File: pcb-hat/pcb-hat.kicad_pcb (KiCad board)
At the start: 4 copper layers, 54.5 x 55 mm, 65 parts, among them Q1 NTMFS5C468NLT1G, Q2 Q_NPN, Q3 Q_PMOS_GSD, U1 AOZ6605PI-1, U2 INA219AxD, U3 INA219AxD, U4 HTD Servo, U5 Vertical_Pi_Breakout, U6 Power_Connector, U7 AOZ6605PI-1, U8 Horizontal_Pi_Breakout, U9 Raspberry_Pi_Generic

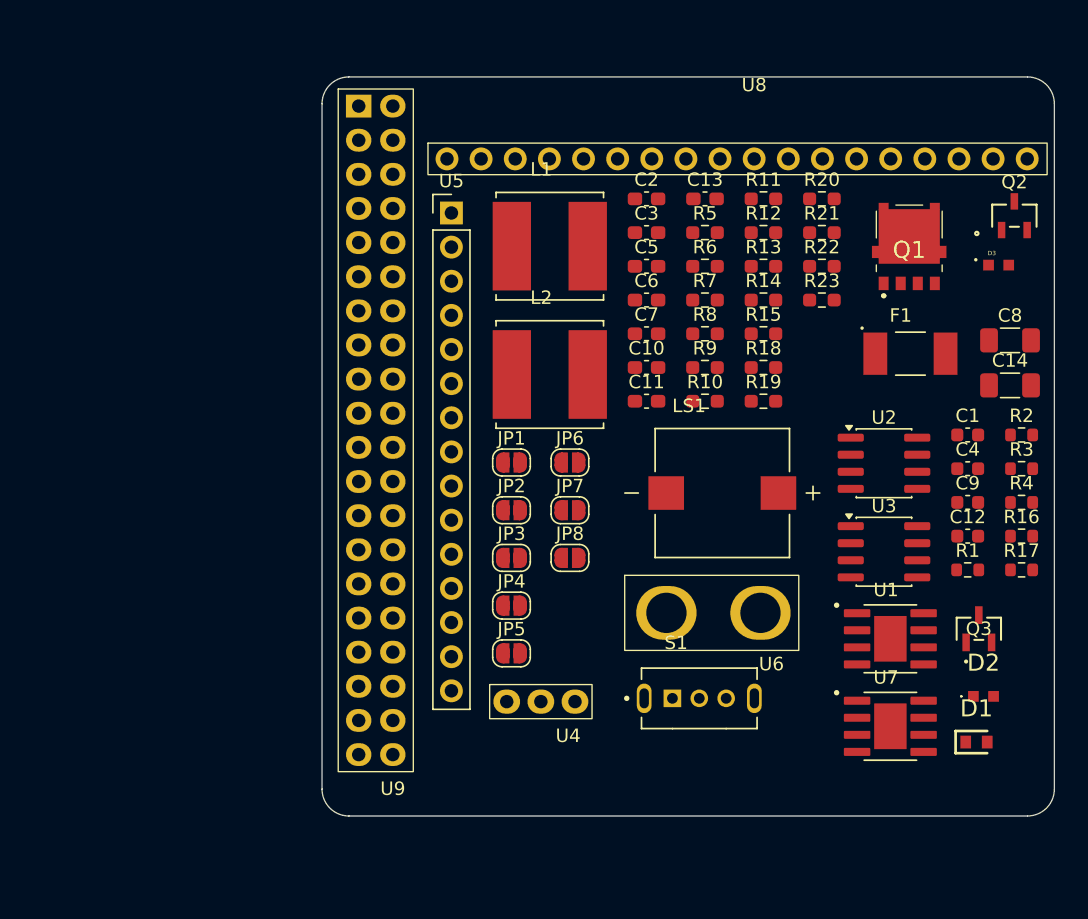
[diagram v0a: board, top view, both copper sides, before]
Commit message: WIP: Fix footprints, add new jumper pad, 3d models. Begin routing
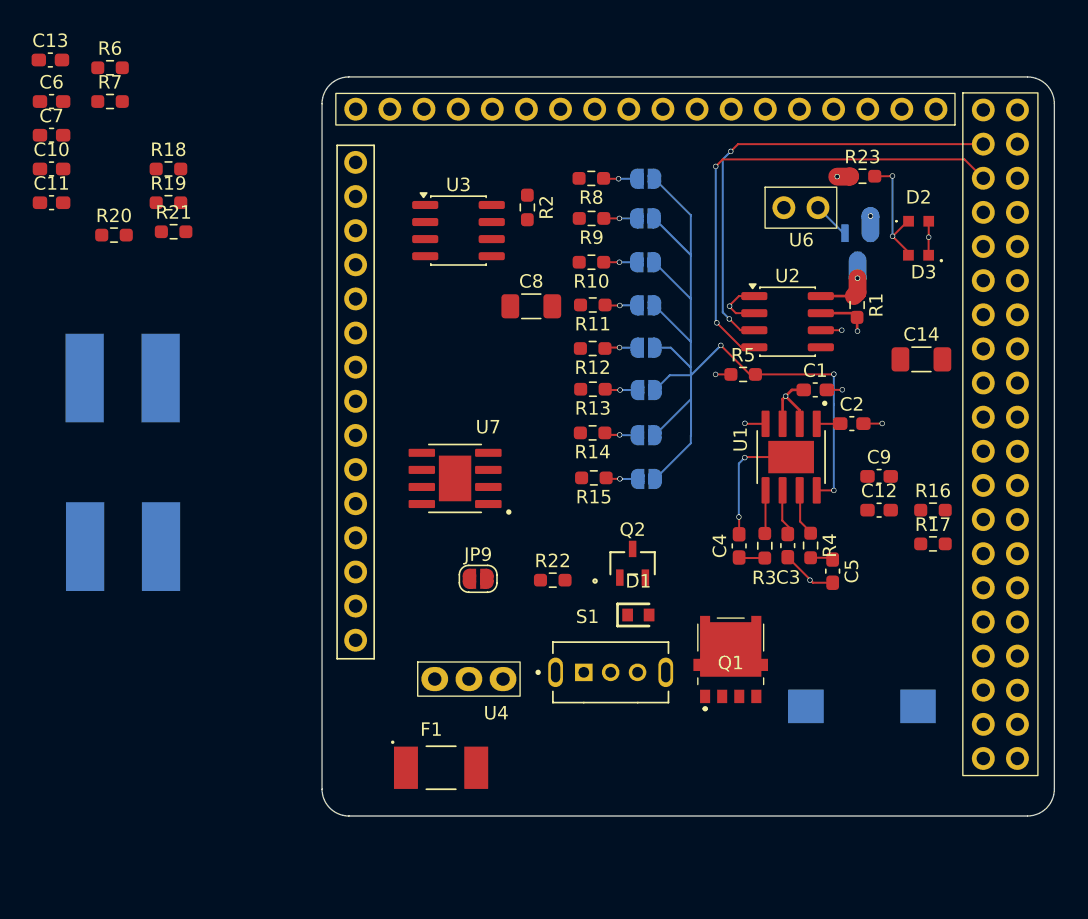
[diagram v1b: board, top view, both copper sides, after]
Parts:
- added JP9: TX to RX?, Jumper:SolderJumper-2_P1.3mm_Open_RoundedPad1.0x1.5mm, F.Cu at (109.1, 100.3)
- C1, C12, C4, C9: footprint Capacitor_SMD:C_0603_1608Metric -> Capacitor_SMD:C_0603_1608Metric_Pad1.08x0.95mm_HandSolder
- JP1, JP2, JP3, JP4, JP5, JP6, JP7, JP8, L1, L2, LS1, Q3: moved to B.Cu
- R1, R16, R17, R2, R3, R4: footprint Resistor_SMD:R_0603_1608Metric -> Resistor_SMD:R_0603_1608Metric_Pad0.98x0.95mm_HandSolder
- U5: footprint Connector_PinHeader_2.54mm:PinHeader_1x15_P2.54mm_Vertical -> pcb_hat:vertical_pi_breakout
- moved R20 52.8 mm to (82.0, 74.8)
- moved C13 49.8 mm to (77.3, 61.7)
- moved R21 48.2 mm to (86.5, 74.5)
- moved U9 47.1 mm to (147.9, 89.4)
- moved C10 46.7 mm to (77.4, 69.8)
- moved C11 46.7 mm to (77.4, 72.4)
- moved C6 46.7 mm to (77.4, 64.8)
- moved C7 46.7 mm to (77.4, 67.3)
- moved R6 46.7 mm to (81.7, 62.3)
- moved R7 46.7 mm to (81.7, 64.8)
- moved R18 46.7 mm to (86.1, 69.8)
- moved R19 46.7 mm to (86.1, 72.4)
- moved F1 46.6 mm to (106.4, 114.4)
- moved R2 40.5 mm to (112.8, 72.7), turned to -90 degrees
- moved U3 39.7 mm to (107.7, 74.4)
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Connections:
- Q2 pad 1: (no net) -> Net-(Q2-B)
- Q2 pad 2: (no net) -> GND
- Q2 pad 3: (no net) -> Net-(D1-A)
- R18 pad 2: Net-(Q2-PadB) -> Net-(Q2-B)
- R19 pad 1: Net-(Q2-PadB) -> Net-(Q2-B)
- R6 pad 2: /Pi_RX_Out -> Net-(JP9-B)
- S1 pad 1: /Pi_RX_Out -> Net-(JP9-B)
- U9 pad 14: (no net) -> GND
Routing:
- net /V_Choose: track 0.00 -> 69.2 mm, vias 0 -> 3
- net /Pi_SCL: track 0.00 -> 35.9 mm, vias 0 -> 2
- net /Pi_SDA: track 0.00 -> 34.4 mm, vias 0 -> 2
- net GND: track 0.00 -> 20.6 mm, vias 0 -> 8
- net VCC_LOAD: track 0.00 -> 10.8 mm, vias 0 -> 2
- net Net-(D2-K): track 0.00 -> 9.37 mm, vias 0 -> 2
- net Net-(U1-LX): track 0.00 -> 9.36 mm, vias 0 -> 2
- net VCC: track 0.00 -> 5.22 mm, vias 0 -> 1
- net Net-(U1-COMP): track 0.00 -> 3.53 mm
- net Net-(U1-VCC): track 0.00 -> 3.51 mm
- net Net-(U1-BST): track 0.00 -> 3.24 mm
- net Net-(JP5-B): track 0.00 -> 2.51 mm, vias 0 -> 1
- net Net-(JP1-B): track 0.00 -> 2.50 mm, vias 0 -> 1
- net Net-(JP7-B): track 0.00 -> 2.49 mm, vias 0 -> 1
- net Net-(JP3-B): track 0.00 -> 2.46 mm, vias 0 -> 1
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- added copper zone on In1.Cu, net +BATT
- added copper zone on In2.Cu, net GND
- added copper zone on In1.Cu, net VCC_LOAD

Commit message: Finish PCB design v0.1
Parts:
- removed the R6 at (81.7, 62.3)
- removed S1: SLW-864587-2A-RA-N-D, pcb_hat:SW_SLW-864587-2A-RA-N-D
- removed the U5 at (100.0, 69.4)
- removed U8: Horizontal_Pi_Breakout, pcb_hat:horizontal_breakout_footprint
- added G***: LOGO, pcb_hat:club_logo, B.Cu at (123.2, 110.4)
- added JP2: Servo Selector, Jumper:SolderJumper-3_P1.3mm_Open_RoundedPad1.0x1.5mm, F.Cu at (135.1, 105.9)
- added R7: 4k7, Resistor_SMD:R_0603_1608Metric_Pad0.98x0.95mm_HandSolder, F.Cu at (141.9, 98.8)
- added RPi5: RPi5, pcb_hat:Raspberry Pi 5, F.Cu at (123.4, 99.6)
- added kibuzzard-694E41B7: G***, kibuzzard-694E41B7, F.Cu at (136.4, 94.0)
- added kibuzzard-694E58A9: G***, kibuzzard-694E58A9, F.Cu at (132.2, 64.7)
- added kibuzzard-694E58BC: G***, kibuzzard-694E58BC, F.Cu at (139.2, 64.7)
- C14, C8: moved to B.Cu
- JP10: renamed from JP8; moved to F.Cu
- JP3: renamed from JP1; moved to F.Cu
- JP4: renamed from JP2; moved to F.Cu
- JP5: renamed from JP3; moved to F.Cu
- JP6: renamed from JP4; moved to F.Cu
- JP7: renamed from JP5; moved to F.Cu
- JP8: renamed from JP6; moved to F.Cu
- JP9: renamed from JP7; moved to F.Cu
- moved R6 76.3 mm to (142.2, 111.3), turned to 90 degrees
- moved C7 71.4 mm to (123.8, 121.6), turned to 180 degrees
- moved C13 65.7 mm to (140.9, 78.1), turned to 180 degrees
- moved C11 64.2 mm to (140.9, 81.6), turned to 180 degrees
- moved L2 58.0 mm to (135.3, 73.5), turned to 90 degrees
- moved R20 57.9 mm to (139.9, 76.2), turned to 180 degrees
- moved C10 52.5 mm to (129.2, 77.7), turned to 180 degrees
- moved R21 50.7 mm to (137.2, 76.2), turned to 90 degrees
- moved C6 50.7 mm to (123.6, 85.8), turned to -90 degrees
- moved U3 48.0 mm to (128.1, 117.8), turned to 90 degrees
- moved R2 42.6 mm to (127.2, 112.8), turned to 0 degrees
- moved L1 40.6 mm to (120.6, 99.8), turned to -90 degrees
- moved D1 33.3 mm to (127.3, 70.3), turned to 180 degrees
- moved R22 31.2 mm to (132.7, 75.0)
- moved JP1 30.9 mm to (139.5, 105.9), turned to 180 degrees
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- renumbered JP9 to JP1, R7 to R6, U6 to U5, U7 to U6, U9 to U7
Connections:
- U7 pad 11: /GPIO17 -> unconnected-(U7-GPIO17/GPIO_GEN0-Pad11)
- U7 pad 13: /GPIO27 -> unconnected-(U7-GPIO27/GPIO_GEN2-Pad13)
- U7 pad 15: /GPIO22 -> unconnected-(U7-GPIO22/GPIO_GEN3-Pad15)
- U7 pad 16: /GPIO23 -> unconnected-(U7-GPIO23/GPIO_GEN4-Pad16)
- U7 pad 18: /GPIO24 -> unconnected-(U7-GPIO24/GPIO_GEN5-Pad18)
- U7 pad 19: /GPIO10 -> unconnected-(U7-GPIO10/SPI_MOSI-Pad19)
- U7 pad 21: /GPIO9 -> unconnected-(U7-GPIO9/SPI_MISO-Pad21)
- U7 pad 22: /GPIO25 -> unconnected-(U7-GPIO25/GPIO_GEN6-Pad22)
- U7 pad 23: /GPIO11 -> unconnected-(U7-GPIO11/SPI_SCLK-Pad23)
- U7 pad 24: /GPIO8 -> unconnected-(U7-GPIO8/~{SPI_CE0}-Pad24)
- U7 pad 26: /GPIO7 -> unconnected-(U7-GPIO7/~{SPI_CE1}-Pad26)
- U7 pad 27: /ID_SD -> unconnected-(U7-ID_SD-Pad27)
- U7 pad 28: /ID_SC -> unconnected-(U7-ID_SC-Pad28)
- U7 pad 31: /GPIO6 -> unconnected-(U7-GPIO6-Pad31)
- U7 pad 32: /GPIO12 -> unconnected-(U7-GPIO12-Pad32)
- U7 pad 33: /GPIO13 -> unconnected-(U7-GPIO13-Pad33)
- U7 pad 35: /GPIO19 -> unconnected-(U7-GPIO19-Pad35)
- U7 pad 36: /GPIO16 -> unconnected-(U7-GPIO16-Pad36)
- U7 pad 38: /GPIO20 -> unconnected-(U7-GPIO20-Pad38)
- U7 pad 40: /GPIO21 -> unconnected-(U7-GPIO21-Pad40)
- U7 pad 7: /GPIO4 -> unconnected-(U7-GPIO4/GPIO_GCKL-Pad7)
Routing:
- net +3V3: track 0.00 -> 146.9 mm, vias 0 -> 2
- net /Pi_SDA: track 34.4 -> 98.6 mm, vias 2 -> 4
- net /Pi_SCL: track 35.9 -> 95.5 mm, vias 2 -> 4
- net VDC_LOAD: track 0.00 -> 49.9 mm, vias 0 -> 4
- net /Pi_RX_Out: track 0.00 -> 45.1 mm, vias 0 -> 2
- net VDC: track 0.00 -> 43.4 mm, vias 0 -> 4
- net /GPIO18: track 0.00 -> 42.3 mm, vias 0 -> 2
- net GND: track 20.6 -> 56.7 mm, vias 8 -> 19
- net +5V: track 0.00 -> 35.9 mm, vias 0 -> 1
- net /V_Choose: track 69.2 -> 37.8 mm, vias 3 -> 0
- net /Pi_TX_Out: track 0.00 -> 30.6 mm, vias 0 -> 1
- net VCC_LOAD: track 10.8 -> 33.7 mm, vias 2 -> 3
- net Net-(D1-A): track 0.00 -> 17.5 mm
- net Net-(JP1-B): track 0.00 -> 10.5 mm
- net /BUZZER_PIN: track 0.00 -> 9.73 mm
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- added copper zone on In2.Cu, net +BATT
- added copper zone on In1.Cu, net GND
- added copper zone on B.Cu, net Net-(U1-LX)
- added copper zone on F.Cu, net Net-(U1-LX)
- added copper zone on B.Cu, net Net-(U6-LX)
- added copper zone on F.Cu, net Net-(U6-LX)
- added copper zone on In2.Cu, net VDC
- removed copper zone on In1.Cu, net +BATT
- removed copper zone on In2.Cu, net GND
- removed copper zone on In1.Cu, net VCC_LOAD
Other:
- board size 54.5 x 55 mm -> 40.9 x 60.1 mm
- board text added: "+"
- board text added: "-"
- board text added: "18V-5A"
- board text added: "Max"
- board text added: "New"
- board text added: "Old"
- board text added: "S"
- board text added: "Servo Voltage Selector"
- board text added: "v0.1"

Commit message: Fix blue LED not turning on
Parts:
- R18: value 10k -> 8.2k
- R19: value 100k -> 1k
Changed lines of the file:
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@@
 			)
 		)
-		(property "Value" "100k"
+		(property "Value" "1k"
 			(at 0 1.43 90)
 			(layer "F.Fab")
@@
 			)
 		)
-		(property "Value" "10k"
+		(property "Value" "8.2k"
 			(at 0 1.43 90)
 			(layer "F.Fab")

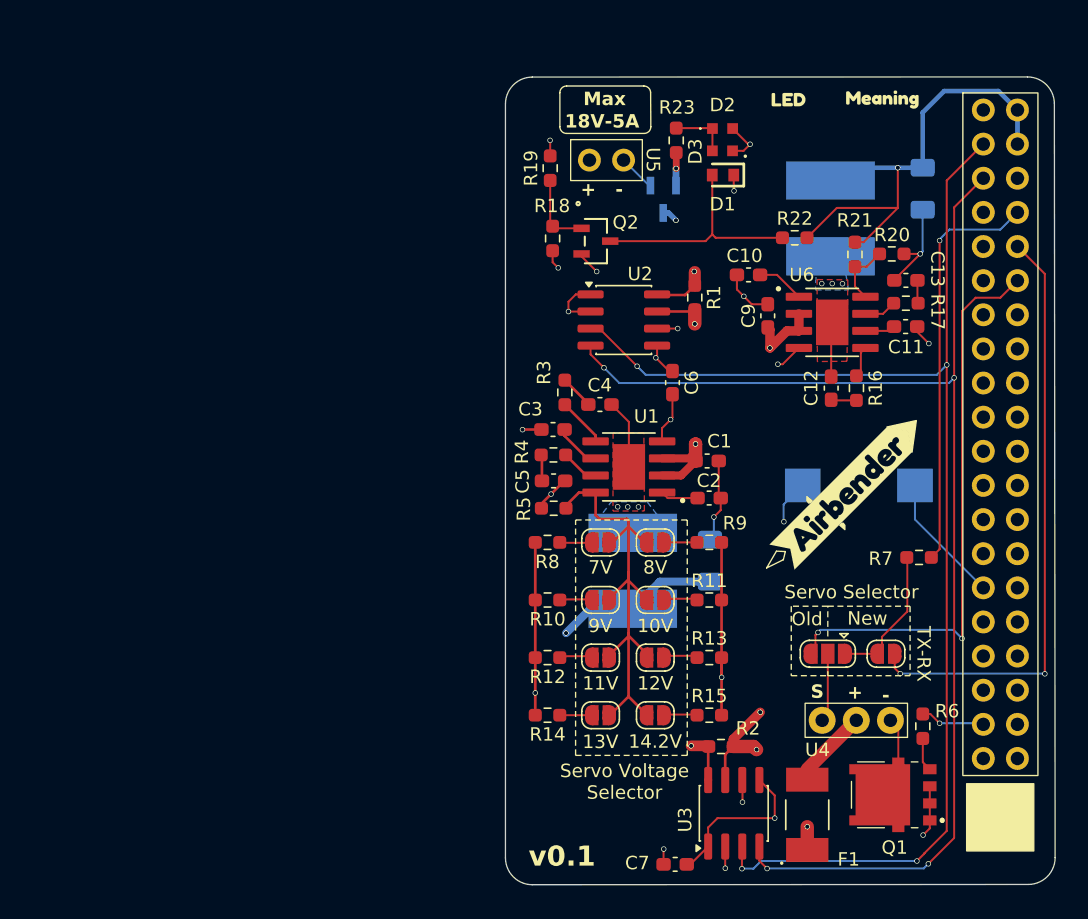
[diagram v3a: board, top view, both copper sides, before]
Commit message: Update schematic and reroute PCB
See the github PR for all changes
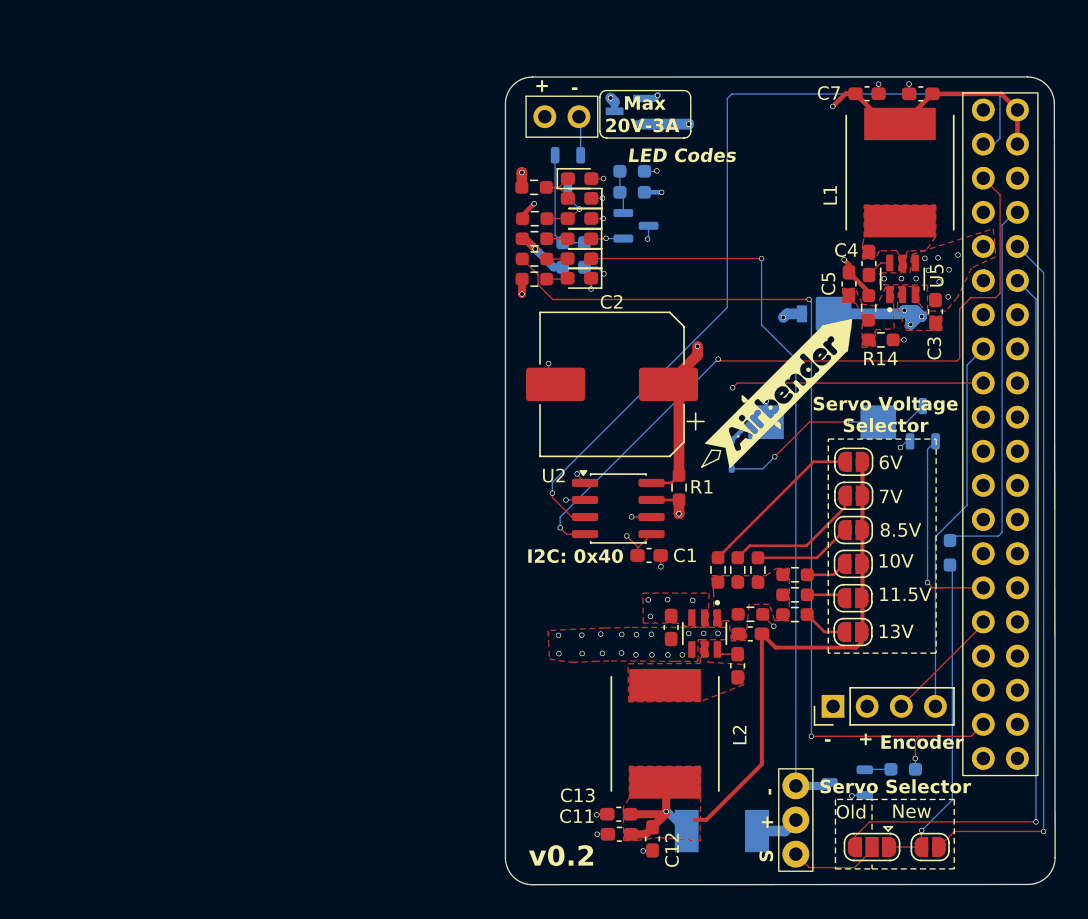
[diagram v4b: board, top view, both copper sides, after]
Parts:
- removed the C1 at (126.2, 91.6)
- removed C14: 47u, Capacitor_SMD:C_1206_3216Metric_Pad1.33x1.80mm_HandSolder
- removed JP10, JP9: SolderJumper_2_Open, Jumper:SolderJumper-2_P1.3mm_Open_RoundedPad1.0x1.5mm
- removed the Q3 at (122.9, 72.1)
- removed the R16 at (137.3, 86.2)
- removed the R17 at (140.9, 79.8)
- removed the R2 at (127.2, 112.8)
- removed the R20 at (139.9, 76.2)
- removed the R21 at (137.2, 76.2)
- removed the R3 at (115.6, 86.5)
- removed the R4 at (114.7, 91.1)
- removed the R5 at (114.7, 95.1)
- removed the U1 at (120.3, 92.0)
- removed the U3 at (128.1, 117.8)
- removed kibuzzard-694E58A9: G***, kibuzzard-694E58A9
- removed kibuzzard-694E58BC: G***, kibuzzard-694E58BC
- added C6: 22u, Capacitor_SMD:C_0603_1608Metric_Pad1.08x0.95mm_HandSolder, F.Cu at (142.1, 64.3)
- added D4: SS3P4-M3/84A, Diode_SMD:D_SMP_DO-220AA, B.Cu at (134.9, 80.6)
- added D5: LED_Small, LED_SMD:LED_0603_1608Metric_Pad1.05x0.95mm_HandSolder, F.Cu at (116.6, 75.0)
- added D6: 1N4148WS, Diode_SMD:D_SOD-323, B.Cu at (128.0, 91.1)
- added D7: LED_Small, LED_SMD:LED_0603_1608Metric_Pad1.05x0.95mm_HandSolder, F.Cu at (116.6, 76.5)
- added D8: LED_Small, LED_SMD:LED_0603_1608Metric_Pad1.05x0.95mm_HandSolder, F.Cu at (116.7, 78.0)
- added Q1: Q_PMOS_GSD, pcb_hat:SOT_7DS-T1-GE3_VIS, B.Cu at (120.3, 65.6)
- added Q4: 2N7002K_R1_00001, Package_TO_SOT_SMD:TSOT-23, B.Cu at (142.2, 88.8)
- added R10: 10k, Resistor_SMD:R_0603_1608Metric_Pad0.98x0.95mm_HandSolder, B.Cu at (120.6, 70.0)
- added R11: 1k, Resistor_SMD:R_0603_1608Metric_Pad0.98x0.95mm_HandSolder, F.Cu at (113.3, 76.5)
- added R12: 2k, Resistor_SMD:R_0603_1608Metric_Pad0.98x0.95mm_HandSolder, F.Cu at (113.3, 78.0)
- added R13: 162k, Resistor_SMD:R_0603_1608Metric_Pad0.98x0.95mm_HandSolder, F.Cu at (138.2, 80.2)
- added R8: 2k, Resistor_SMD:R_0603_1608Metric_Pad0.98x0.95mm_HandSolder, F.Cu at (113.3, 75.0)
- added R9: 9.1k, Resistor_SMD:R_0603_1608Metric_Pad0.98x0.95mm_HandSolder, B.Cu at (120.6, 71.6)
- added U4: TL431DBZ, Package_TO_SOT_SMD:SOT-23, B.Cu at (120.9, 74.1)
- added U5: AP63300WU-7, pcb_hat:SOT95P280X100-6N, F.Cu at (140.7, 78.0)
- added U7: AP63300WU-7, pcb_hat:SOT95P280X100-6N, F.Cu at (126.0, 104.4)
- C10: value 22n -> 12p
- C11: value 1u -> 22u
- C12: value 0.1u -> 22u
- C13: value 0.012u -> 22u
- C2: value 22n -> 1000u; footprint Capacitor_SMD:C_0603_1608Metric_Pad1.08x0.95mm_HandSolder -> Capacitor_SMD:CP_Elec_10x10.5
- C3: value 1u -> 10u
- C4: value 0.1u -> 100n
- C5: value 0.012u -> 47p
- C7: value 100n -> 22u
- C8: value 47u -> 10u; footprint Capacitor_SMD:C_1206_3216Metric_Pad1.33x1.80mm_HandSolder -> Capacitor_SMD:C_0603_1608Metric_Pad1.08x0.95mm_HandSolder; moved to F.Cu
- C9: value 22u -> 100n
- D1: renamed from D2; footprint pcb_hat:LEDLSQ97601N1Q21 -> LED_SMD:LED_0603_1608Metric_Pad1.05x0.95mm_HandSolder
- D2: renamed from D3; footprint pcb_hat:LEDM1608X80 -> LED_SMD:LED_0603_1608Metric_Pad1.05x0.95mm_HandSolder
- D3: renamed from D1; footprint pcb_hat:LEDC1608X35N -> LED_SMD:LED_0603_1608Metric_Pad1.05x0.95mm_HandSolder
- F1: moved to B.Cu
- L1, L2: value SRN8040TA-4R7M -> 6.8u; footprint pcb_hat:IND_SRN8040TA-4R7M -> pcb_hat:IND_ETQP4M6R8KVK; moved to F.Cu
- LS1: value SMI-1027-T-5V-R -> ~
- Q2: footprint pcb_hat:MTR_MMBT2222A-TP_MCE -> Package_TO_SOT_SMD:TSOT-23; moved to B.Cu
- Q3: renamed from Q1; value NTMFS5C468NLT1G -> PJA3404A_R1_00001; footprint pcb_hat:NRVTS10100EMFST1G -> Package_TO_SOT_SMD:TSOT-23; moved to B.Cu
- R14: value 310k -> 30.1k
- R15: value 340k -> 30.1k
- R16: renamed from R8; value 160k -> 196k
- R17: renamed from R9; value 184k -> 233k
- R18: renamed from R10; value 210k -> 290k
- R19: renamed from R11; value 235k -> 346k
- R20: renamed from R12; value 260k -> 403k
- R21: renamed from R13; value 285k -> 459k
- R3: renamed from R18; moved to B.Cu
- R4: renamed from R19; moved to B.Cu
- R6: renamed from R7; moved to B.Cu
- R7: renamed from R6; moved to B.Cu
- U1: renamed from U5; value Power_Connector -> Headers
- U6: value AOZ6605PI-1 -> ~; footprint pcb_hat:SOIC127P600X170-9N -> Connector_PinHeader_2.54mm:PinHeader_1x04_P2.54mm_Vertical
- moved C7 59.1 mm to (138.1, 64.2), turned to 0 degrees
- moved C13 45.1 mm to (119.6, 117.9)
- moved C11 43.4 mm to (119.6, 119.4)
- moved L2 40.3 mm to (123.0, 111.9), turned to -90 degrees
- moved R14 37.4 mm to (139.1, 82.6), turned to 0 degrees
- moved C12 36.1 mm to (122.1, 119.7), turned to -90 degrees
- moved L1 35.7 mm to (140.5, 70.1), turned to 90 degrees
- moved C3 29.8 mm to (143.2, 80.5), turned to 90 degrees
- moved U6 28.6 mm to (135.5, 109.8), turned to 90 degrees
- moved C10 26.7 mm to (129.4, 104.5)
- moved C5 26.4 mm to (136.7, 78.4), turned to -90 degrees
- moved C9 26.1 mm to (128.4, 106.8), turned to -90 degrees
- moved C4 22.6 mm to (138.2, 76.9), turned to 90 degrees
- moved JP3 19.8 mm to (137.1, 91.6), turned to 0 degrees
- moved JP5 19.5 mm to (137.1, 96.7), turned to 0 degrees
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- renumbered C6 to C1, R23 to R2, R22 to R5, U4 to U3, U7 to U8
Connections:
- C10 pad 1: Net-(U6-SS) -> VDC
- C10 pad 2: GND -> /V_Choose
- C11 pad 1: GND -> VDC
- C11 pad 2: Net-(U6-VCC) -> GND
- C12 pad 1: Net-(C12-Pad1) -> VDC
- C12 pad 2: Net-(U6-LX) -> GND
- C13 pad 1: Net-(C13-Pad1) -> VDC
- C2 pad 1: Net-(U1-SS) -> VCC
- C3 pad 1: GND -> Net-(D4-K)
- C3 pad 2: Net-(U1-VCC) -> GND
- C5 pad 1: Net-(C5-Pad1) -> +5V
- C5 pad 2: GND -> Net-(U5-FB)
- C7 pad 1: +3V3 -> +5V
- C8 pad 1: GND -> VCC_LOAD
- C8 pad 2: VDC -> GND
- C9 pad 1: VDC_LOAD -> Net-(U7-BST)
- C9 pad 2: GND -> Net-(U7-SW)
- F1 pad 1: VDC_LOAD -> VDC
- JP3 pad 1: /V_Choose -> Net-(JP3-A)
- JP3 pad 2: Net-(JP3-B) -> VDC
- JP4 pad 1: /V_Choose -> Net-(JP4-A)
- JP4 pad 2: Net-(JP4-B) -> VDC
- JP5 pad 1: /V_Choose -> Net-(JP5-A)
- JP5 pad 2: Net-(JP5-B) -> VDC
- JP6 pad 1: /V_Choose -> Net-(JP6-A)
- JP6 pad 2: Net-(JP6-B) -> VDC
- JP7 pad 1: /V_Choose -> Net-(JP7-A)
- JP7 pad 2: Net-(JP7-B) -> VDC
- JP8 pad 1: /V_Choose -> Net-(JP8-A)
- JP8 pad 2: Net-(JP8-B) -> VDC
- L1 pad 2: VDC -> +5V
- L2 pad 1: Net-(U6-LX) -> Net-(U7-SW)
- L2 pad 2: +5V -> VDC
- Q3 pad 1: GND -> Net-(Q3-G)
- Q3 pad 3: GND -> /Servo_Control
- R14 pad 1: Net-(JP9-B) -> Net-(U5-FB)
- R14 pad 2: VDC -> GND
- R15 pad 1: Net-(JP10-B) -> /V_Choose
- R15 pad 2: VDC -> GND
- R16 pad 1: Net-(JP3-B) -> /V_Choose
- R16 pad 2: VDC -> Net-(JP3-A)
- R17 pad 1: Net-(JP4-B) -> /V_Choose
- R17 pad 2: VDC -> Net-(JP4-A)
- R18 pad 1: Net-(JP5-B) -> /V_Choose
- R18 pad 2: VDC -> Net-(JP5-A)
- R19 pad 1: Net-(JP6-B) -> /V_Choose
- R19 pad 2: VDC -> Net-(JP6-A)
- R20 pad 1: Net-(JP7-B) -> /V_Choose
- R20 pad 2: VDC -> Net-(JP7-A)
- R21 pad 1: Net-(JP8-B) -> /V_Choose
- R21 pad 2: VDC -> Net-(JP8-A)
- R7 pad 1: Net-(Q1-G) -> Net-(Q3-G)
- U6 pad 1: Net-(U6-SS) -> GND
- U6 pad 2: VDC_LOAD -> +5V
- U6 pad 3: VDC_LOAD -> /GPIO6
- U6 pad 4: GND -> /GPIO22
- U8 pad 15: unconnected-(U7-GPIO22/GPIO_GEN3-Pad15) -> /GPIO22
- U8 pad 29: /BUZZER_PIN -> /GPIO5
- U8 pad 31: unconnected-(U7-GPIO6-Pad31) -> /GPIO6
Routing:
- net +3V3: track 146.9 -> 58.3 mm
- net +5V: track 35.9 -> 115.1 mm, vias 1 -> 5
- net /GPIO26: track 4.82 -> 71.4 mm, vias 1 -> 3
- net VDC: track 43.4 -> 94.2 mm, vias 4 -> 2
- net VDC_LOAD: track 49.9 -> 0.00 mm, vias 4 -> 0
- net /Servo_Control: track 5.79 -> 55.6 mm, vias 0 -> 1
- net /Pi_SCL: track 95.5 -> 53.8 mm, vias 4 -> 2
- net /V_Choose: track 37.8 -> 0.00 mm
- net /Pi_SDA: track 98.6 -> 63.2 mm, vias 4 -> 1
- net VCC_LOAD: track 33.7 -> 68.8 mm, vias 3 -> 7
- net GND: track 56.7 -> 24.1 mm, vias 19 -> 49
- net /GPIO22: track 0.00 -> 28.1 mm
- net VCC: track 9.72 -> 32.3 mm
- net Net-(D6-A): track 0.00 -> 16.2 mm, vias 0 -> 2
- net /GPIO5: track 0.00 -> 15.1 mm, vias 0 -> 1
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- added copper zone on F.Cu, net /V_Choose
- added copper zone on F.Cu, net GND
- added copper zone on F.Cu, net Net-(D4-K)
- added copper zone on F.Cu, net Net-(U5-FB)
- added copper zone on F.Cu, net Net-(U7-SW)
- added copper zone on F.Cu, net VCC_LOAD
- added copper zone on F.Cu, net VDC
- removed copper zone on B.Cu, net Net-(U5-SW)
- removed copper zone on B.Cu, net Net-(U6-LX)
- removed copper zone on F.Cu, net Net-(U6-LX)
- removed copper zone on In2.Cu, net VDC
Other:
- board text added: "20V-3A"
- board text added: "Encoder"
- board text added: "I2C: 0x40"
- board text added: "LED Codes"
- board text added: "v0.2"
- board text removed: "18V-5A"
- board text removed: "v0.1"
